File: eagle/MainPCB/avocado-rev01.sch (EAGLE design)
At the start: 65 parts, among them J1 10118194-0001LF, J2 CON-DSUB-15-VGA, J3 0475710001, P2 CONNECTOR-15686115148922, P3 PADTH, U1 V3S, U2 AP65111A, U3 AP65111A, U4 AP65111A

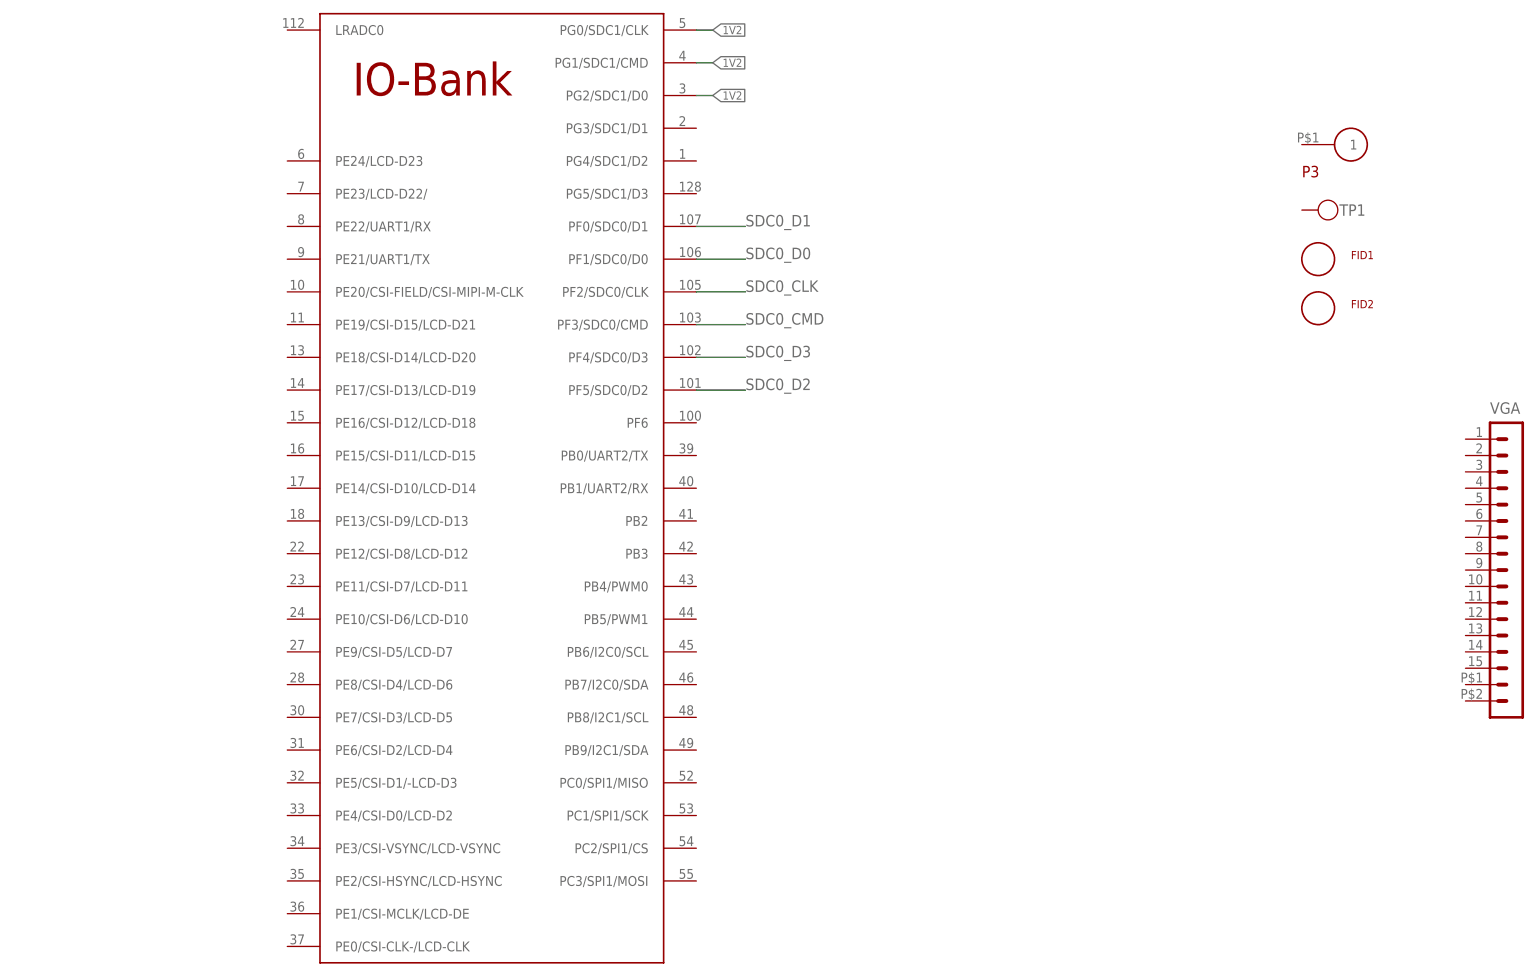
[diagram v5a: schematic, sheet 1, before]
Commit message: added testpoints
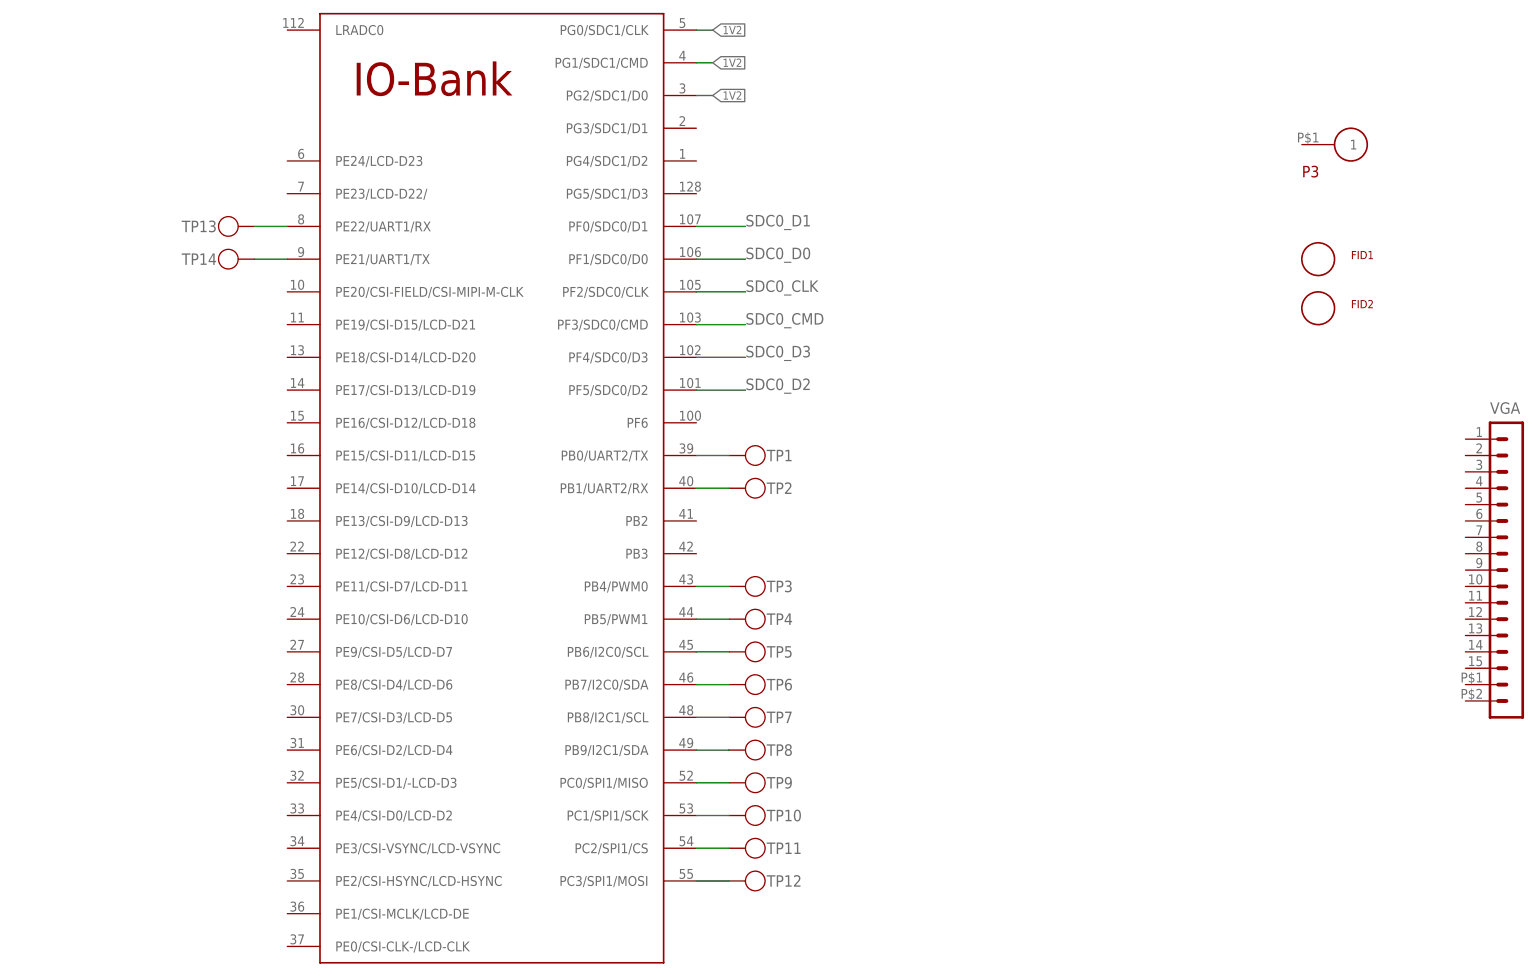
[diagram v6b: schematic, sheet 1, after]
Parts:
- added C21: 10u, marius:C0603
- added TP10, TP11, TP12, TP13, TP14, TP2, TP3, TP4, TP5, TP6, TP7, TP8, TP9: TEST_TESTPOINT, marius:TEST_TESTPOINT
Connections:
- new net N$47: TP1.2, U1G$2.PB0/UART2/TX
- new net N$48: TP2.2, U1G$2.PB1/UART2/RX
- new net N$49: TP5.2, U1G$2.PB6/I2C0/SCL
- new net N$50: TP6.2, U1G$2.PB7/I2C0/SDA
- new net N$51: TP7.2, U1G$2.PB8/I2C1/SCL
- new net N$52: TP8.2, U1G$2.PB9/I2C1/SDA
- new net N$53: TP9.2, U1G$2.PC0/SPI1/MISO
- new net N$54: TP10.2, U1G$2.PC1/SPI1/SCK
- new net N$55: TP11.2, U1G$2.PC2/SPI1/CS
- new net N$56: TP12.2, U1G$2.PC3/SPI1/MOSI
- new net N$57: TP3.2, U1G$2.PB4/PWM0
- new net N$58: TP4.2, U1G$2.PB5/PWM1
- new net N$59: TP14.2, U1G$2.PE21/UART1/TX
- new net N$60: TP13.2, U1G$2.PE22/UART1/RX
- net GND: now also C21.2
- net VCC: now also C21.1
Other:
- moved on the sheet: TP1

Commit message: updated i2c
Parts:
- removed P3: PADTH, marius:PADTH
- added 5V, GND: PADTH, marius:PADTH
- added R27: (no value), resistor:R-EU_R0603
- added R28, R29, R30, R31: 2k, resistor:R-EU_R0603
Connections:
- new net N$61: D1.COMM_ANODE
- new net N$62: D2.COMM_ANODE
- new net N$63: R27.1, R28.1, R29.1, R30.1, R31.1
- net GND: now also GND.1
- net N$49: now also R27.2, R28.2
- net N$50: now also R29.2
- net N$51: now also R30.2
- net N$52: now also R31.2
- net VCC: now also 5V.1; no longer D1.COMM_ANODE, D2.COMM_ANODE

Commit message: updated i2c
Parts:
- removed R31: 2k, resistor:R-EU_R0603
- R27: value (none) -> 2k
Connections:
- net N$49: no longer R28.2
- net N$50: now also R28.2; no longer R29.2
- net N$51: now also R29.2; no longer R30.2
- net N$52: now also R30.2; no longer R31.2
- net N$63: no longer R31.1
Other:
- moved on the sheet: R28, R29, R30
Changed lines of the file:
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@@
 <part name="TP13" library="marius" library_urn="urn:adsk.eagle:library:5910807" deviceset="TEST_TESTPOINT" device="" package3d_urn="urn:adsk.eagle:package:5911110/1"/>
 <part name="TP14" library="marius" library_urn="urn:adsk.eagle:library:5910807" deviceset="TEST_TESTPOINT" device="" package3d_urn="urn:adsk.eagle:package:5911110/1"/>
-<part name="R27" library="resistor" library_urn="urn:adsk.eagle:library:348" deviceset="R-EU_" device="R0603" package3d_urn="urn:adsk.eagle:package:26057/1"/>
+<part name="R27" library="resistor" library_urn="urn:adsk.eagle:library:348" deviceset="R-EU_" device="R0603" package3d_urn="urn:adsk.eagle:package:26057/1" value="2k"/>
 <part name="R28" library="resistor" library_urn="urn:adsk.eagle:library:348" deviceset="R-EU_" device="R0603" package3d_urn="urn:adsk.eagle:package:26057/1" value="2k"/>
 <part name="R29" library="resistor" library_urn="urn:adsk.eagle:library:348" deviceset="R-EU_" device="R0603" package3d_urn="urn:adsk.eagle:package:26057/1" value="2k"/>
 <part name="R30" library="resistor" library_urn="urn:adsk.eagle:library:348" deviceset="R-EU_" device="R0603" package3d_urn="urn:adsk.eagle:package:26057/1" value="2k"/>
-<part name="R31" library="resistor" library_urn="urn:adsk.eagle:library:348" deviceset="R-EU_" device="R0603" package3d_urn="urn:adsk.eagle:package:26057/1" value="2k"/>
 <part name="5V" library="marius" library_urn="urn:adsk.eagle:library:5910807" deviceset="PAD" device="TH" package3d_urn="urn:adsk.eagle:package:5911125/1"/>
 <part name="GND" library="marius" library_urn="urn:adsk.eagle:library:5910807" deviceset="PAD" device="TH" package3d_urn="urn:adsk.eagle:package:5911125/1"/>
@@
 <instance part="R27" gate="G$1" x="139.7" y="71.12" smashed="yes" rot="R180">
 <attribute name="NAME" x="143.51" y="69.6214" size="1.778" layer="95" rot="R180"/>
-<attribute name="VALUE" x="143.51" y="74.422" size="1.778" layer="96" rot="R180"/>
-</instance>
-<instance part="R28" gate="G$1" x="139.7" y="71.12" smashed="yes" rot="R180">
-<attribute name="NAME" x="143.51" y="69.6214" size="1.778" layer="95" rot="R180"/>
-<attribute name="VALUE" x="143.51" y="74.422" size="1.778" layer="96" rot="R180"/>
-</instance>
-<instance part="R29" gate="G$1" x="139.7" y="66.04" smashed="yes" rot="R180">
+<attribute name="VALUE" x="148.59" y="71.882" size="1.778" layer="96" rot="R180"/>
+</instance>
+<instance part="R28" gate="G$1" x="139.7" y="66.04" smashed="yes" rot="R180">
 <attribute name="NAME" x="143.51" y="64.5414" size="1.778" layer="95" rot="R180"/>
-<attribute name="VALUE" x="143.51" y="69.342" size="1.778" layer="96" rot="R180"/>
-</instance>
-<instance part="R30" gate="G$1" x="139.7" y="60.96" smashed="yes" rot="R180">
+<attribute name="VALUE" x="148.59" y="66.802" size="1.778" layer="96" rot="R180"/>
+</instance>
+<instance part="R29" gate="G$1" x="139.7" y="60.96" smashed="yes" rot="R180">
 <attribute name="NAME" x="143.51" y="59.4614" size="1.778" layer="95" rot="R180"/>
-<attribute name="VALUE" x="143.51" y="64.262" size="1.778" layer="96" rot="R180"/>
-</instance>
-<instance part="R31" gate="G$1" x="139.7" y="55.88" smashed="yes" rot="R180">
+<attribute name="VALUE" x="148.59" y="61.722" size="1.778" layer="96" rot="R180"/>
+</instance>
+<instance part="R30" gate="G$1" x="139.7" y="55.88" smashed="yes" rot="R180">
 <attribute name="NAME" x="143.51" y="54.3814" size="1.778" layer="95" rot="R180"/>
-<attribute name="VALUE" x="143.51" y="59.182" size="1.778" layer="96" rot="R180"/>
+<attribute name="VALUE" x="148.59" y="56.642" size="1.778" layer="96" rot="R180"/>
 </instance>
 </instances>
@@
 <junction x="121.92" y="73.66"/>
 <pinref part="R27" gate="G$1" pin="2"/>
-<pinref part="R28" gate="G$1" pin="2"/>
-<junction x="134.62" y="71.12"/>
 </segment>
 </net>
@@
 <wire x1="121.92" y1="66.04" x2="134.62" y2="66.04" width="0.1524" layer="91"/>
 <junction x="121.92" y="68.58"/>
-<pinref part="R29" gate="G$1" pin="2"/>
+<pinref part="R28" gate="G$1" pin="2"/>
 </segment>
 </net>
@@
 <junction x="121.92" y="63.5"/>
 <wire x1="121.92" y1="60.96" x2="134.62" y2="60.96" width="0.1524" layer="91"/>
-<pinref part="R30" gate="G$1" pin="2"/>
+<pinref part="R29" gate="G$1" pin="2"/>
 </segment>
 </net>
@@
 <wire x1="121.92" y1="55.88" x2="134.62" y2="55.88" width="0.1524" layer="91"/>
 <junction x="121.92" y="58.42"/>
-<pinref part="R31" gate="G$1" pin="2"/>
+<pinref part="R30" gate="G$1" pin="2"/>
 </segment>
 </net>
@@
 <segment>
 <pinref part="R27" gate="G$1" pin="1"/>
-<pinref part="R28" gate="G$1" pin="1"/>
-<pinref part="R31" gate="G$1" pin="1"/>
+<pinref part="R30" gate="G$1" pin="1"/>
 <wire x1="144.78" y1="55.88" x2="144.78" y2="60.96" width="0.1524" layer="91"/>
 <junction x="144.78" y="71.12"/>
-<pinref part="R29" gate="G$1" pin="1"/>
+<pinref part="R28" gate="G$1" pin="1"/>
 <wire x1="144.78" y1="60.96" x2="144.78" y2="66.04" width="0.1524" layer="91"/>
 <wire x1="144.78" y1="66.04" x2="144.78" y2="71.12" width="0.1524" layer="91"/>
 <junction x="144.78" y="66.04"/>
-<pinref part="R30" gate="G$1" pin="1"/>
+<pinref part="R29" gate="G$1" pin="1"/>
 <junction x="144.78" y="60.96"/>
 <wire x1="144.78" y1="71.12" x2="144.78" y2="73.66" width="0.1524" layer="91"/>
